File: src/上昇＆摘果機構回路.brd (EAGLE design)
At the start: 97.6 x 76.1 mm, 76 parts, among them SW2 SS-12SDP2, T1 2SC3325-Y,LF, T2 2SC3325, U1 MCP2517FD, X1 32.768K12.5PI/MC306, X2 RH100-24.000-18-1020-EXT-TR, X3 XRCGB40M000F4M01R0

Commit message: 3rd fix
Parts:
- removed C10, C9: GRM0335C1H6R0BA01D, GRM0335C1H6R0BA01D:GRM0335C1H120GA01
- removed C6, C7, C8: GCM188L81H104KA57, GCM188L81H104K57(0.1uF):GCM188L81H104KA57
- removed JP2, JP3, JP4: (no value), pinhead:1X02
- removed JP5, JP6: (no value), pinhead:1X04
- removed R4: 120Ω, CR0603:CR0603
- removed R5: 0, CR0603:CR0603
- removed R6, R7: 150, CR0603:CR0603
- removed R8: 10k, CR0603:CR0603
- removed R9: 5.1k, CR0603:CR0603
- removed RJ45_3: MTJ-88ARX1-LH, MTJ-88ARX1-LH:MTJ-88ARX1-LH
- removed SW2: SS-12SDP2, SS-12SDP2:SS-12SDP2
- removed T2: 2SC3325, 2SC3325:2SC3325
- removed U$3: MCP2558FD, MCP2558FD:MCP2558FD
- removed U1: MCP2517FD, MCP2517FD:MCP2517FD
- removed X3: XRCGB40M000F4M01R0, XRCGB40M000F4M01R0:XRCGB40M000F4M00R0
- added LEFT, RIGHT: (no value), pinhead:1X02
- added LEFT2, RIGHT2: (no value), pinhead:1X04
- moved R12 18.4 mm to (23.6, 9.40)
- moved U$8 18.4 mm to (23.4, 12.1)
- moved AZUSA_CTRL1 11.2 mm to (38.7, 9.37)
- moved CTRL 11.2 mm to (47.6, 9.37)
- moved R1 11.2 mm to (42.6, 16.8)
- moved T1 11.2 mm to (37.6, 16.6)
- moved C5 1.34 mm to (57.8, 28.5)
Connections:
- removed net CAN_H: R4.RIGHT, RJ45_3.5, RJ45_3.6, U$3.CANH
- removed net CAN_L: RJ45_3.3, RJ45_3.4, SW2.C, U$3.CANL
- removed net N$12: U$3.TXD, U1.TXCAN
- removed net N$13: U$3.RXD, U1.RXCAN
- removed net N$14: R4.LEFT, SW2.R
- removed net N$15: C9.1, U1.OSC1, X3.1
- removed net N$16: C10.1, R5.RIGHT, X3.2
- removed net N$17: R5.LEFT, U1.OSC2
- removed net N$18: R6.LEFT, RJ45_3.LED2_A
- removed net N$20: JP2.2, U$3.S
- removed net N$21: R7.RIGHT, RJ45_3.LED1_A
- removed net N$24: RJ45_3.LED1_K, T2.C
- removed net N$29: R8.RIGHT, R9.LEFT, T2.B
- net +3V3: no longer C6.P$2, C8.P$1, U$3.VIO, U1.VDD
- net +5V: now also LEFT2.4; no longer C7.P$1, JP5.4, R6.RIGHT, R7.LEFT, RJ45_3.1, RJ45_3.7, U$3.VDD
- net COM_LED: now also LEFT2.3; no longer JP5.3, R9.RIGHT
- net CS: now also RIGHT2.1; no longer JP6.1, U1.NCS
- net MISO: now also RIGHT2.2; no longer JP6.2, U1.SDO
- net MOSI: now also RIGHT2.3; no longer JP6.3, U1.SDI
- net SCK: now also RIGHT2.4; no longer JP6.4, U1.SCK
- net SGND: now also LEFT.1, LEFT.2, LEFT2.1, RIGHT.1, RIGHT.2; no longer C10.2, C6.P$1, C7.P$2, C8.P$2, C9.2, JP2.1, JP3.1, JP3.2, JP4.1, JP4.2, JP5.1, R8.LEFT, RJ45_3.2, RJ45_3.8, RJ45_3.LED2_K, T2.E, U$3.EP, U$3.VSS, U1.VSS
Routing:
- net +3V3: track 228.1 -> 147.6 mm
- net +5V: track 223.7 -> 164.6 mm, vias 3 -> 0
- net SCK: track 26.6 -> 54.7 mm
- net COM_LED: track 34.7 -> 11.5 mm, vias 2 -> 1
- net CS: track 17.8 -> 40.1 mm
- net CAN_L: track 18.8 -> 0.00 mm
- net CAN_H: track 18.8 -> 0.00 mm
- net COM_LED2: track 4.74 -> 22.6 mm
- net N$12: track 15.0 -> 0.00 mm
- net MISO: track 27.3 -> 41.9 mm
- net N$13: track 12.7 -> 0.00 mm
- net MOSI: track 32.6 -> 43.5 mm
- net N$24: track 7.38 -> 0.00 mm
- net N$16: track 7.32 -> 0.00 mm
- net N$20: track 7.23 -> 0.00 mm
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
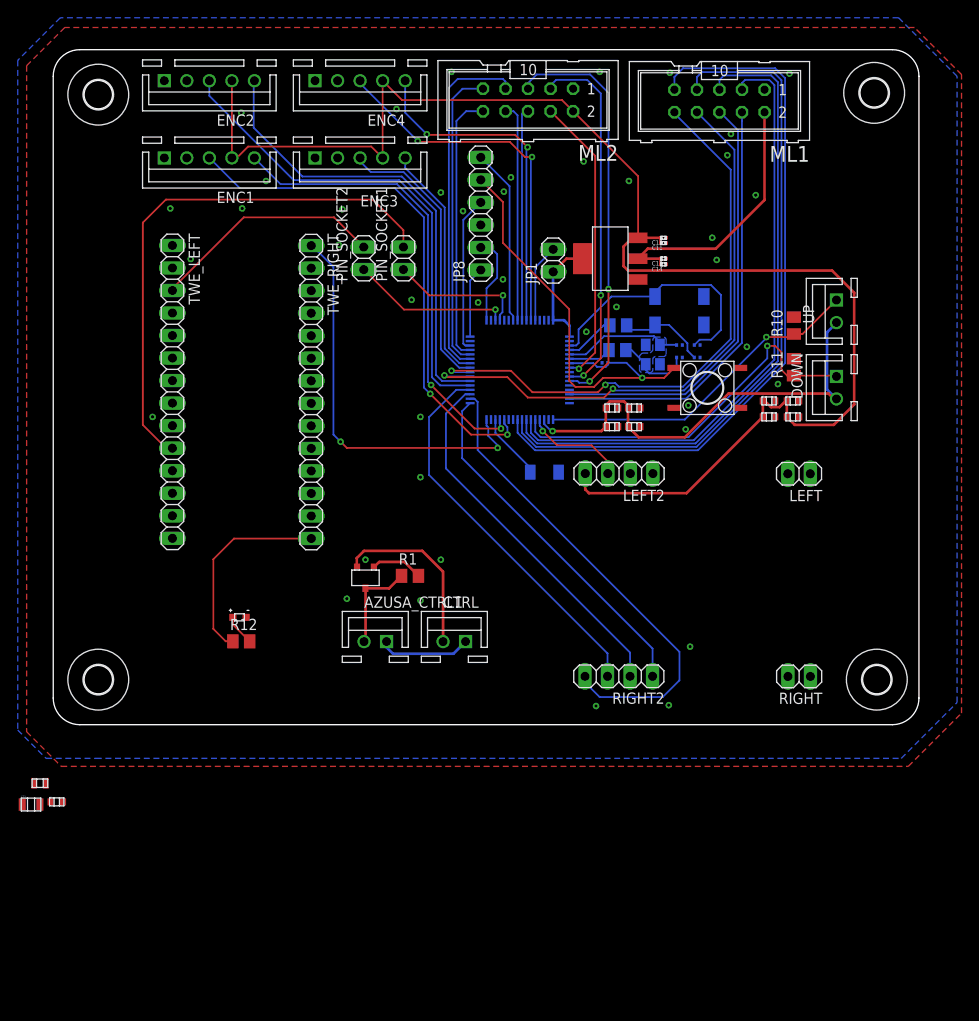
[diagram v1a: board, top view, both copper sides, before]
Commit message: DRC fix
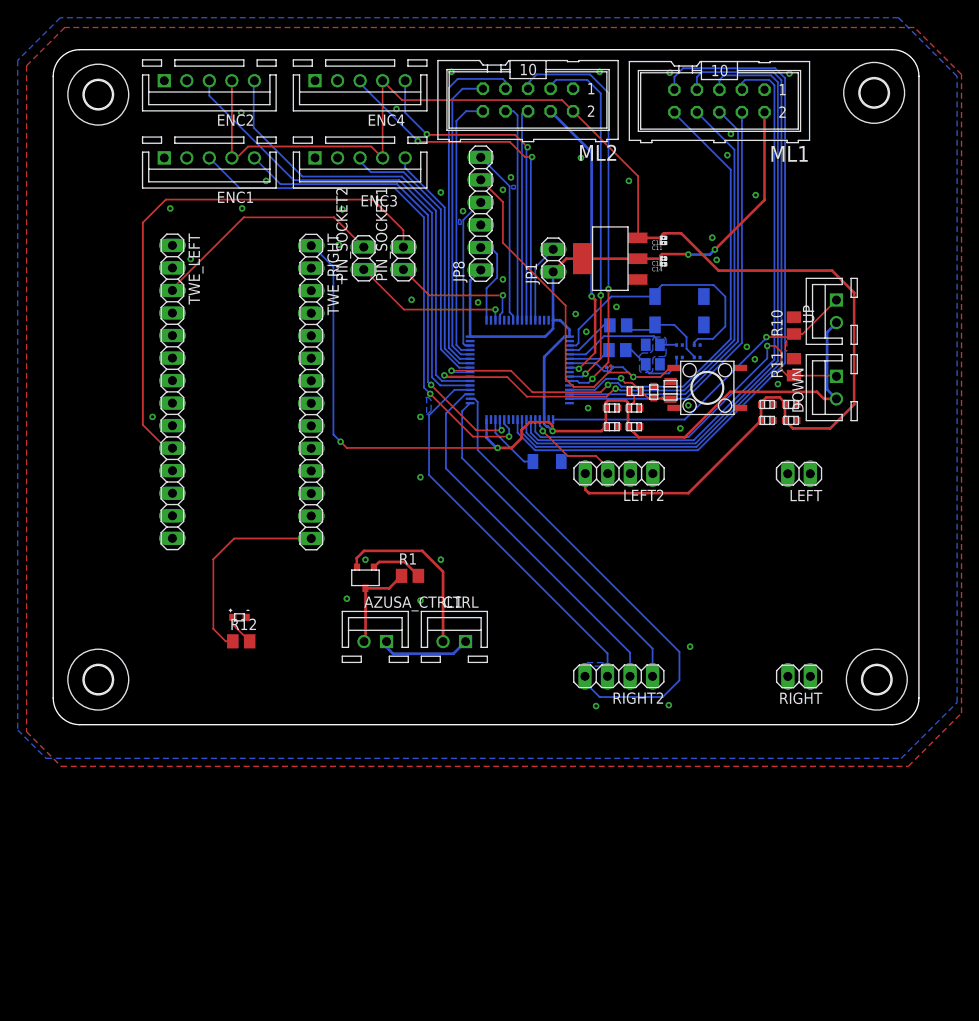
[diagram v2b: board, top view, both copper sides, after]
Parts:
- moved C23 85.9 mm to (72.0, 37.7), turned to 90 degrees
- moved C24 81.6 mm to (70.1, 37.5), turned to 90 degrees
- moved FB1 80.3 mm to (68.0, 37.6)
- moved C5 1.24 mm to (58.1, 29.7)
- moved 0.1μ 0.71 mm to (65.1, 40.3)
- moved C18 0.45 mm to (85.6, 34.3)
- moved C17 0.45 mm to (85.6, 36.1)
- moved C16 0.45 mm to (82.9, 34.3)
- moved C15 0.45 mm to (82.9, 36.1)
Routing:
- net +3V3: track 147.6 -> 184.6 mm, vias 3 -> 5
- net N$46: track 0.00 -> 13.0 mm, vias 0 -> 1
- net +5V: track 164.6 -> 158.3 mm
- net N$3: track 29.2 -> 30.0 mm
- net EN1_A: track 59.6 -> 60.2 mm
- net NRST: track 49.2 -> 48.6 mm
- net LED1: vias 1 -> 2
